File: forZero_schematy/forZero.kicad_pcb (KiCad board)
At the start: 2 copper layers, 70 x 70 mm, 96 parts, among them IC1 NCV21872DMR2G, IC2 MCP4661-103E_ST, IC3 STM32F105RBT6, IC4 AP7347DQ-33W5-7, IC5 MCP2562-E_SN, J1 USB_C_Receptacle_USB2.0_16P, J2 43045-0800, J3 43045-0621, J4 43045-0400, J5 Barrel_Jack_Switch, Q1 AO3400A, Q10 AO3400A, Q2 AO3400A, Q3 AO3400A, Q4 AO3400A, Q5 AO3400A, Q6 AO3400A, Q7 AO3400A, Q8 AO3400A, Q9 AO3400A, Y1 25MHz

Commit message: Wprowadzenie poprawek PCB
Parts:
- added C26: 100n, Capacitor_SMD:C_0805_2012Metric_Pad1.18x1.45mm_HandSolder, F.Cu at (119.3, 75.9)
- added Q11: AO3400A, Package_TO_SOT_SMD:SOT-23, F.Cu at (122.5, 75.8)
- added R42: 100R, Resistor_SMD:R_0805_2012Metric_Pad1.20x1.40mm_HandSolder, F.Cu at (119.3, 79.9)
- added R43: 9.1k, Resistor_SMD:R_0805_2012Metric_Pad1.20x1.40mm_HandSolder, F.Cu at (123.7, 79.9)
- added R44: 9.1k, Resistor_SMD:R_0805_2012Metric_Pad1.20x1.40mm_HandSolder, F.Cu at (130.4, 86.8)
- added R45: 9.1k, Resistor_SMD:R_0805_2012Metric_Pad1.20x1.40mm_HandSolder, F.Cu at (103.3, 79.9)
- added R46: 9.1k, Resistor_SMD:R_0805_2012Metric_Pad1.20x1.40mm_HandSolder, F.Cu at (94.3, 79.9)
- added R47: 9.1k, Resistor_SMD:R_0805_2012Metric_Pad1.20x1.40mm_HandSolder, F.Cu at (103.4, 86.8)
- added R48: 9.1k, Resistor_SMD:R_0805_2012Metric_Pad1.20x1.40mm_HandSolder, F.Cu at (94.2, 86.8)
- added R49: 9.1k, Resistor_SMD:R_0805_2012Metric_Pad1.20x1.40mm_HandSolder, F.Cu at (112.4, 86.8)
- added R50: 9.1k, Resistor_SMD:R_0805_2012Metric_Pad1.20x1.40mm_HandSolder, F.Cu at (112.5, 79.9)
- added R51: 9.1k, Resistor_SMD:R_0805_2012Metric_Pad1.20x1.40mm_HandSolder, F.Cu at (121.4, 86.8)
- added R52: 9.1k, Resistor_SMD:R_0805_2012Metric_Pad1.20x1.40mm_HandSolder, F.Cu at (121.5, 79.9)
- R18, R19, R21, R23, R25, R27, R29, R31: value 1k -> 100R
- moved Q3 20.4 mm to (131.4, 90.8)
- moved R18 20.1 mm to (128.2, 90.8)
- moved R17 16.2 mm to (132.6, 86.8), turned to -90 degrees
- moved C10 12.8 mm to (128.2, 86.8), turned to -90 degrees
- moved C25 11.0 mm to (122.8, 101.6), turned to -90 degrees
- moved C24 10.2 mm to (114.6, 102.0)
- moved RESET1 9.68 mm to (131.2, 101.0)
- moved BOOT1 9.68 mm to (131.2, 111.6)
- moved R34 9.68 mm to (124.8, 112.8)
- moved R35 9.48 mm to (125.0, 101.6)
- moved R6 8.44 mm to (106.5, 129.4)
- moved J1 8.18 mm to (74.1, 103.5)
- moved C1 8.15 mm to (93.9, 127.0)
- moved C18 8.15 mm to (118.4, 108.7)
- moved C19 8.15 mm to (118.4, 106.5)
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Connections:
- net CLUSTER_BREAK_PADS renamed CLUSTER_BRAKE_PADS
- C10 pad 1: Net-(Q3-G) -> GND
- C10 pad 2: GND -> Net-(Q3-G)
- C12 pad 1: Net-(Q5-G) -> GND
- C12 pad 2: GND -> Net-(Q5-G)
- C13 pad 1: Net-(Q6-G) -> GND
- C13 pad 2: GND -> Net-(Q6-G)
- C14 pad 1: Net-(Q7-G) -> GND
- C14 pad 2: GND -> Net-(Q7-G)
- C15 pad 1: Net-(Q8-G) -> GND
- C15 pad 2: GND -> Net-(Q8-G)
- C16 pad 1: Net-(Q9-G) -> GND
- C16 pad 2: GND -> Net-(Q9-G)
- C17 pad 1: Net-(Q10-G) -> GND
- C17 pad 2: GND -> Net-(Q10-G)
- F1 pad 2: 5V_USB -> Net-(F1-Pad2)
- IC3 pad 22: SENSOR -> unconnected-(IC3-PA6-Pad22)
- IC3 pad 24: unconnected-(IC3-PC4-Pad24) -> TCR
- IC3 pad 25: unconnected-(IC3-PC5-Pad25) -> BRAKE_PADS
- IC3 pad 26: BREAK_PADS -> ABS
- IC3 pad 27: ABS -> unconnected-(IC3-PB1-Pad27)
- IC3 pad 29: unconnected-(IC3-PB10-Pad29) -> SENSOR
- J1 pad A4: 5V_USB -> Net-(F1-Pad2)
- J1 pad A9: 5V_USB -> Net-(F1-Pad2)
- J1 pad B4: 5V_USB -> Net-(F1-Pad2)
- J1 pad B9: 5V_USB -> Net-(F1-Pad2)
- J2 pad 4: unconnected-(J2-Pad4) -> CLUSTER_SENSOR
- J2 pad 8: CLUSTER_SENSOR -> CLUSTER_TCR
- R25 pad 1: BREAK_PADS -> BRAKE_PADS
- R39 pad 1: 5V_USB -> 5V
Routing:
- net TCR: track 0.00 -> 29.3 mm
- net 5V_USB: track 19.0 -> 0.00 mm
- net CLUSTER_SPEED: track 8.06 -> 26.5 mm
- net CLUSTER_CAN_L: track 56.3 -> 71.6 mm
- net CLUSTER_CAN_H: track 59.0 -> 74.2 mm
- net CLUSTER_TCR: track 0.00 -> 15.0 mm
- net Net-(F1-Pad2): track 0.00 -> 14.8 mm
- net 5V: track 86.9 -> 98.6 mm
- net BRAKE_PADS: track 0.00 -> 11.0 mm
- net 3V3: track 173.6 -> 184.2 mm
- net BREAK_PADS: track 9.29 -> 0.00 mm
- net GND: track 111.2 -> 119.4 mm, vias 59 -> 138
- net CLUSTER_AIR_BAG: track 11.3 -> 19.3 mm
- net CLUSTER_TEMP_LVL: track 74.5 -> 82.5 mm
- net CLUSTER_FUEL_LVL: track 118.8 -> 126.8 mm
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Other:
- board size 70 x 70 mm -> 74.2 x 80 mm
- board text added: "1- TCR 2- SENSOR 3- BRAKE PADS 4- ABS 5- COOL LVL 6- AIR BAG 7- WIPER FLUID 8- BRAKES"
- board text added: "Analog section"
- board text added: "CAN section"
- board text added: "Cluster driver"
- board text added: "M.Ratajczak"
- board text added: "Tell-tales and speed"
- board text added: "USB and LDO"
- board text added: "designed by"
- board text added: "forZero"
- board text removed: "1- SENSOR 2- N/A 3- BREAK PADS 4- ABS 5- COOL LVL 6- AIR BAG 7- WIPER FLUID 8- BREAKS"
- board text removed: "MR2026"
- board text removed: "for Zero"

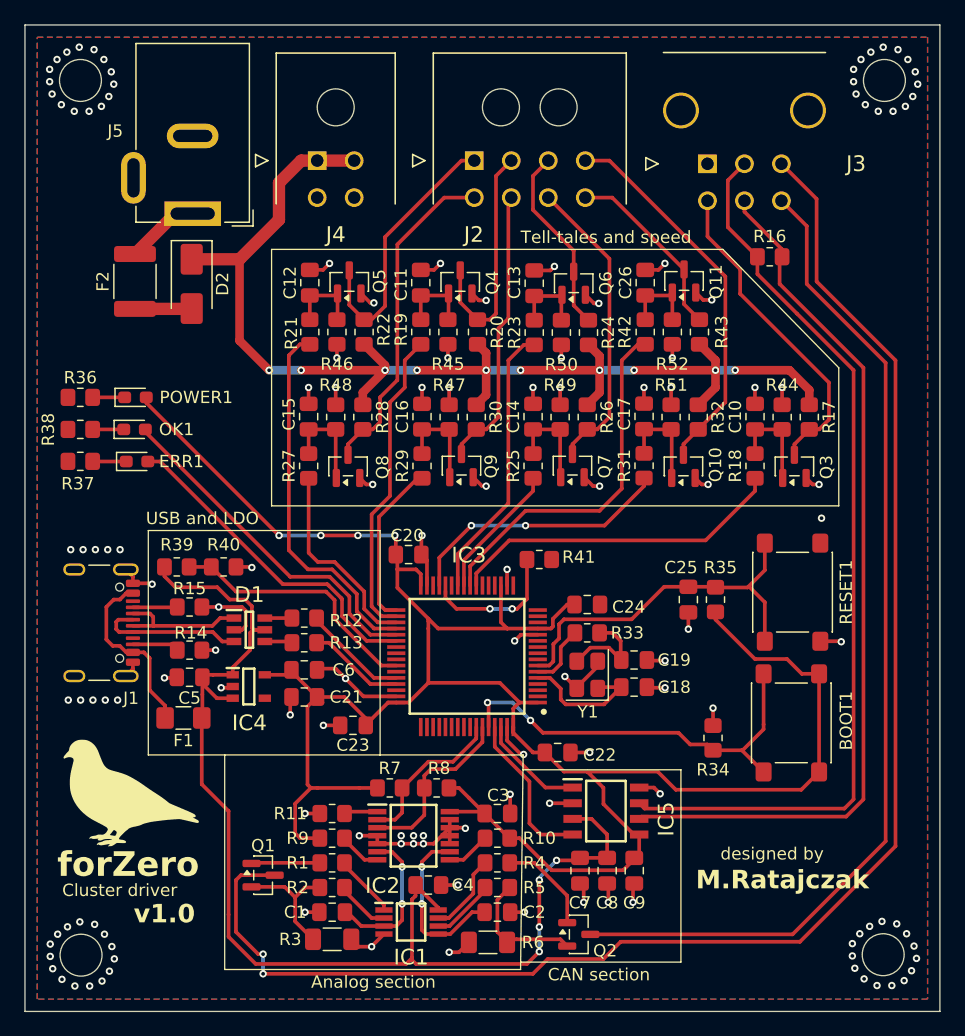
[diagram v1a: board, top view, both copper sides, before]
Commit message: Wykonano finalne PCB dla forZero_1v0
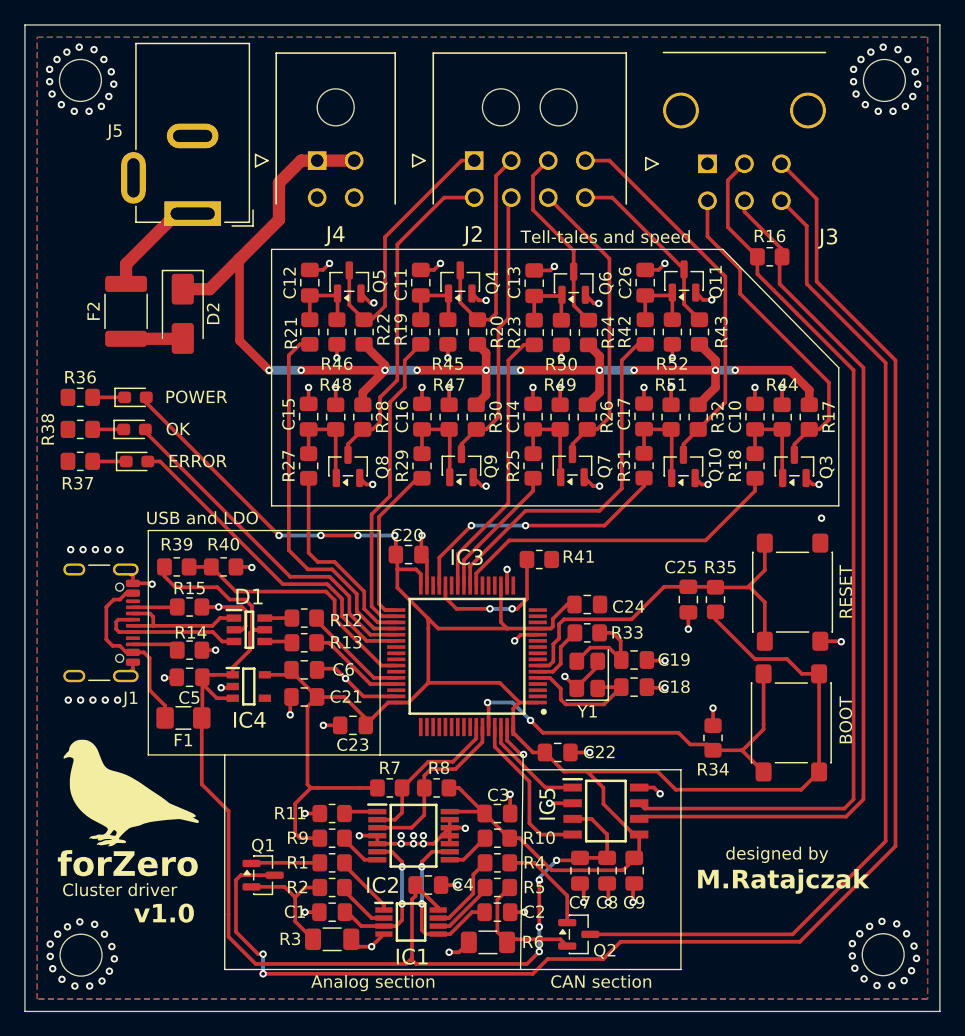
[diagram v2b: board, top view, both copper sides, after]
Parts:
- moved D2 2.53 mm to (81.8, 78.4)
- moved F2 2.53 mm to (77.2, 78.2)
- renumbered BOOT1 to BOOT, ERR1 to ERROR, OK1 to OK, POWER1 to POWER, RESET1 to RESET
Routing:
- net Net-(F2-Pad1): track 6.03 -> 10.1 mm
- net 12V: track 97.4 -> 99.2 mm
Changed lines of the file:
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@@
 			(plot_on_all_layers_selection 0x00000000_00000000_00000000_00000000)
 			(disableapertmacros no)
-			(usegerberextensions no)
+			(usegerberextensions yes)
 			(usegerberattributes yes)
 			(usegerberadvancedattributes yes)
@@
 			(outputformat 1)
 			(mirror no)
-			(drillshape 1)
+			(drillshape 0)
 			(scaleselection 1)
-			(outputdirectory "")
+			(outputdirectory "C:/PSIO/ForZero/forZero_schematy/Gerber/")
 		)
 	)
@@
 	(net 99 "Net-(POWER1-K)")
 	(net 100 "VBUS")
-	(net 101 "Net-(ERR1-K)")
+	(net 101 "Net-(ERROR1-K)")
 	(net 102 "Net-(OK1-K)")
 	(net 103 "Net-(IC3-PB2)")
@@
 		(descr "Tactile switch, 6x6 mm, H4.3 mm, gullwing terminals, https://www.ckswitches.com/media/1471/pts645.pdf")
 		(tags "SPST Button Switch CK C&K")
-		(property "Reference" "RESET1"
+		(property "Reference" "RESET"
 			(at 0 -4.35 90)
 			(layer "F.SilkS")
@@
 		(tags "Integrated Circuit")
 		(property "Reference" "IC4"
-			(at 0.05 2.95 0)
+			(at 0.05 2.75 0)
 			(layer "F.SilkS")
 			(effects
@@
 		)
 		(fp_text user "${REFERENCE}"
-			(at 0.05 2.95 0)
+			(at 0.05 2.75 0)
 			(layer "F.Fab")
 			(effects
@@
 			(layers "F.Cu" "F.Mask" "F.Paste")
 			(roundrect_rratio 0.208333)
-			(net 101 "Net-(ERR1-K)")
+			(net 101 "Net-(ERROR1-K)")
 			(pintype "passive")
 		)
@@
 		(tags "capacitor handsolder")
 		(property "Reference" "C22"
-			(at 3.4 0.2 0)
+			(at 3.4 0 0)
 			(layer "F.SilkS")
 			(effects
@@
 		(descr "LED SMD 0603 (1608 Metric), square (rectangular) end terminal, IPC-7351 nominal, (Body size source: http://www.tortai-tech.com/upload/download/2011102023233369053.pdf), generated with kicad-footprint-generator")
 		(tags "LED handsolder")
-		(property "Reference" "OK1"
-			(at 3.4 0 0)
+		(property "Reference" "OK"
+			(at 3.5125 0 0)
 			(layer "F.SilkS")
 			(effects
@@
 		(descr "LED SMD 0603 (1608 Metric), square (rectangular) end terminal, IPC-7351 nominal, (Body size source: http://www.tortai-tech.com/upload/download/2011102023233369053.pdf), generated with kicad-footprint-generator")
 		(tags "LED handsolder")
-		(property "Reference" "POWER1"
+		(property "Reference" "POWER"
 			(at 4.925 0 0)
 			(layer "F.SilkS")
@@
 	(footprint "Fuse:Fuse_1812_4532Metric_Pad1.30x3.40mm_HandSolder"
 		(layer "F.Cu")
-		(at 77.92175 75.8 -90)
+		(at 77.2 78.225 -90)
 		(descr "Fuse SMD 1812 (4532 Metric), square (rectangular) end terminal, IPC-7351 nominal with elongated pad for handsoldering. (Body size source: https://www.nikhef.nl/pub/departments/mt/projects/detectorR_D/dtddice/ERJ2G.pdf), generated with kicad-footprint-generator")
 		(tags "fuse handsolder")
@@
 		(tags "Integrated Circuit")
 		(property "Reference" "IC1"
-			(at 0 2.85 0)
+			(at 0.088 2.85 0)
 			(layer "F.SilkS")
 			(effects
@@
 		)
 		(fp_text user "${REFERENCE}"
-			(at 0 2.85 0)
+			(at 0.088 2.85 0)
 			(layer "F.Fab")
 			(effects
@@
 		(descr "Tactile switch, 6x6 mm, H4.3 mm, gullwing terminals, https://www.ckswitches.com/media/1471/pts645.pdf")
 		(tags "SPST Button Switch CK C&K")
-		(property "Reference" "BOOT1"
+		(property "Reference" "BOOT"
 			(at 0.18 4.45 90)
 			(layer "F.SilkS")
@@
 	(footprint "Diode_SMD:D_SMA"
 		(layer "F.Cu")
-		(at 82.52175 76 -90)
+		(at 81.8 78.425 -90)
 		(descr "Diode SMA (DO-214AC)")
 		(tags "Diode SMA (DO-214AC)")
@@
 		(tags "Integrated Circuit")
 		(property "Reference" "IC5"
-			(at 4.888 0.65 90)
+			(at -4.712 -0.55 90)
 			(layer "F.SilkS")
 			(effects
@@
 		)
 		(fp_text user "${REFERENCE}"
-			(at 4.888 0.65 90)
+			(at -4.712 -0.55 90)
 			(layer "F.Fab")
 			(effects
@@
 		(tags "Integrated Circuit")
 		(property "Reference" "IC3"
-			(at -0.15 8.2 180)
+			(at 0 8 180)
 			(layer "F.SilkS")
 			(effects
@@
 		)
 		(fp_text user "${REFERENCE}"
-			(at -0.15 8.2 180)
+			(at 0 8 180)
 			(layer "F.Fab")
 			(effects
@@
 		(descr "LED SMD 0603 (1608 Metric), square (rectangular) end terminal, IPC-7351 nominal, (Body size source: http://www.tortai-tech.com/upload/download/2011102023233369053.pdf), generated with kicad-footprint-generator")
 		(tags "LED handsolder")
-		(property "Reference" "ERR1"
-			(at 3.6 0 0)
+		(property "Reference" "ERROR"
+			(at 4.9125 0 0)
 			(layer "F.SilkS")
 			(effects
@@
 			(layers "F.Cu" "F.Mask" "F.Paste")
 			(roundrect_rratio 0.25)
-			(net 101 "Net-(ERR1-K)")
+			(net 101 "Net-(ERROR1-K)")
 			(pinfunction "K")
 			(pintype "passive")
@@
 		(tags "Diode")
 		(property "Reference" "D1"
-			(at 0 -2.85 0)
+			(at 0 -2.65 0)
 			(layer "F.SilkS")
 			(effects
@@
 		)
 		(fp_text user "${REFERENCE}"
-			(at 0 -2.85 0)
+			(at 0 -2.65 0)
 			(layer "F.Fab")
 			(effects
@@
 		(tags "Connector")
 		(property "Reference" "J3"
-			(at -12.05 0 180)
+			(at -9.85 -5.9446 180)
 			(layer "F.SilkS")
 			(effects
@@
 		)
 		(fp_text user "${REFERENCE}"
-			(at 0 0 180)
+			(at -9.85 -5.9446 180)
 			(layer "F.Fab")
 			(effects
@@
 		(layer "F.Mask")
 	)
+	(gr_circle
+		(center 138.6 130.4)
+		(end 141.7241 130.4)
+		(stroke
+			(width 0.1)
+			(type solid)
+		)
+		(fill yes)
+		(layer "B.Mask")
+	)
+	(gr_circle
+		(center 73.5241 59.5241)
+		(end 76.6482 59.5241)
+		(stroke
+			(width 0.1)
+			(type solid)
+		)
+		(fill yes)
+		(layer "B.Mask")
+	)
+	(gr_circle
+		(center 73.573212 130.461891)
+		(end 76.697312 130.461891)
+		(stroke
+			(width 0.1)
+			(type solid)
+		)
+		(fill yes)
+		(layer "B.Mask")
+	)
+	(gr_circle
+		(center 138.7241 59.5241)
+		(end 141.8482 59.5241)
+		(stroke
+			(width 0.1)
+			(type solid)
+		)
+		(fill yes)
+		(layer "B.Mask")
+	)
 	(gr_line
 		(start 89 73.2)
@@
 	)
 	(gr_line
-		(start 109.2 131)
-		(end 122.2 131)
+		(start 109.2 131.6)
+		(end 122.2 131.6)
 		(stroke
 			(width 0.1)
@@
 	(gr_line
 		(start 122.2 115.4)
-		(end 122.2 131)
+		(end 122.2 131.6)
 		(stroke
 			(width 0.1)
@@
 	)
 	(gr_text "CAN section"
-		(at 111.4 132.6 0)
+		(at 111.6 133.2 0)
 		(layer "F.SilkS")
 		(effects
@@
 	)
 	(gr_text "designed by"
-		(at 125.4 122.8 0)
+		(at 125.8 122.8 0)
 		(layer "F.SilkS")
 		(effects
@@
 	)
 	(gr_text "POWER 12V"
-		(at 86.6 75 0)
+		(at 86.2 75 0)
 		(layer "B.SilkS")
 		(effects
@@
 	)
 	(segment
-		(start 77.92175 78.025)
-		(end 82.49675 78.025)
+		(start 77.2 80.45)
+		(end 81.775 80.45)
 		(width 1)
 		(layer "F.Cu")
@@
 	)
 	(segment
-		(start 82.49675 78.025)
-		(end 82.52175 78)
+		(start 81.775 80.45)
+		(end 81.8 80.425)
 		(width 1)
 		(layer "F.Cu")
@@
 	)
 	(segment
-		(start 82.52175 74)
-		(end 86.4 74)
-		(width 1)
-		(layer "F.Cu")
-		(net 91)
-	)
-	(segment
 		(start 98.2 83)
 		(end 98.2 82.6)
@@
 	)
 	(segment
+		(start 83.975 76.425)
+		(end 86.4 74)
+		(width 1)
+		(layer "F.Cu")
+		(net 91)
+	)
+	(segment
 		(start 132.60625 84.60625)
 		(end 132.60625 85.8)
@@
 	)
 	(segment
+		(start 81.8 76.425)
+		(end 83.975 76.425)
+		(width 1)
+		(layer "F.Cu")
+		(net 91)
+	)
+	(segment
 		(start 86.4 74)
 		(end 89.6 70.8)
@@
 	)
 	(segment
-		(start 81.19675 70.3)
-		(end 77.92175 73.575)
+		(start 77.2 74.4)
+		(end 77.2 76)
+		(width 1)
+		(layer "F.Cu")
+		(net 92)
+	)
+	(segment
+		(start 82.6 70.3)
+		(end 81.3 70.3)
 		(width 1)
 		(layer "F.Cu")
@@
 		(width 1)
 		(layer "F.Cu")
+		(net 92)
+	)
+	(segment
+		(start 81.3 70.3)
+		(end 77.2 74.4)
+		(width 1)
+		(layer "F.Cu")
